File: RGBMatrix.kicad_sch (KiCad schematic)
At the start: 245 parts, among them Q17 PNP, Q18 PNP, Q19 PNP, Q20 PNP, Q21 PNP, Q22 PNP, Q23 PNP, Q24 PNP, Q25 PNP, Q26 PNP, Q27 PNP, Q28 PNP, Q29 PNP, Q30 PNP, Q31 PNP, Q32 PNP, U1 74LS596, U2 74LS596, U3 74LS596, U4 74LS596, U5 74LS596, U6 74LS596, U8 74LS596, U9 74LS596

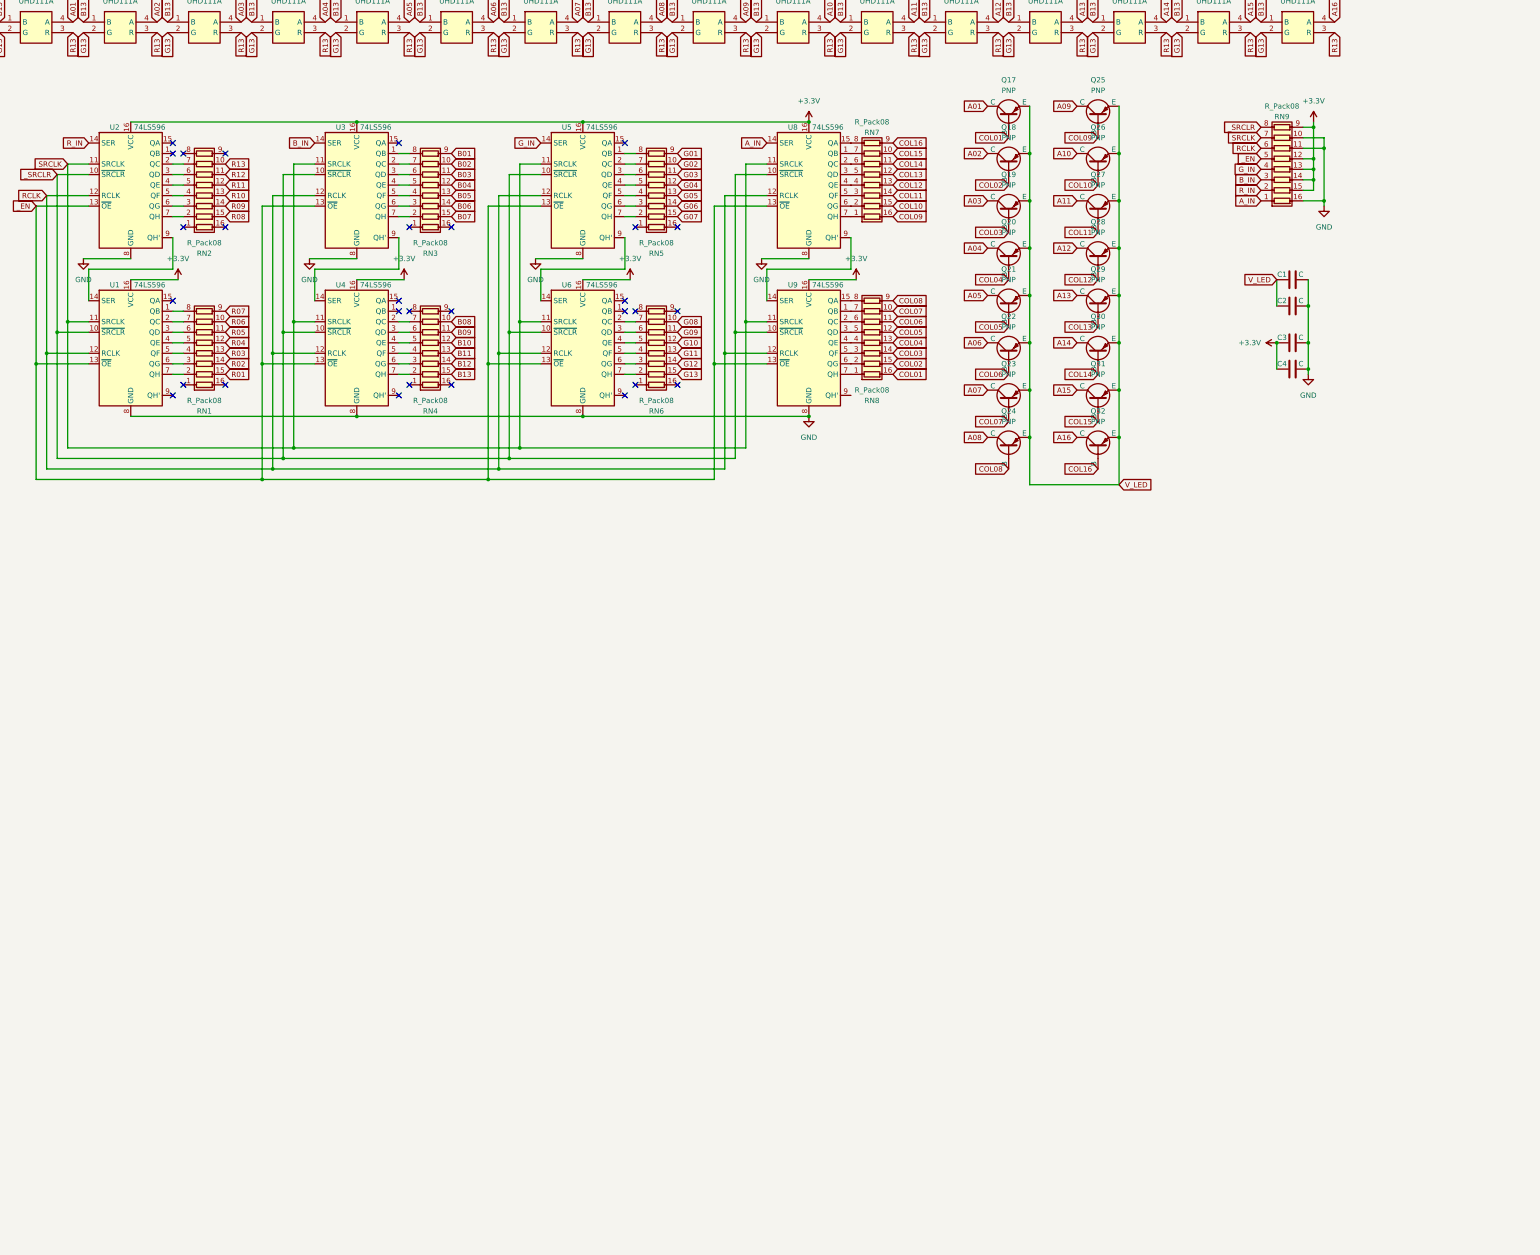
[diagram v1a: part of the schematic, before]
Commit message: High side switch, capacitors
replace fet-s with high side switches
added capacitors for every Shift Register power pin
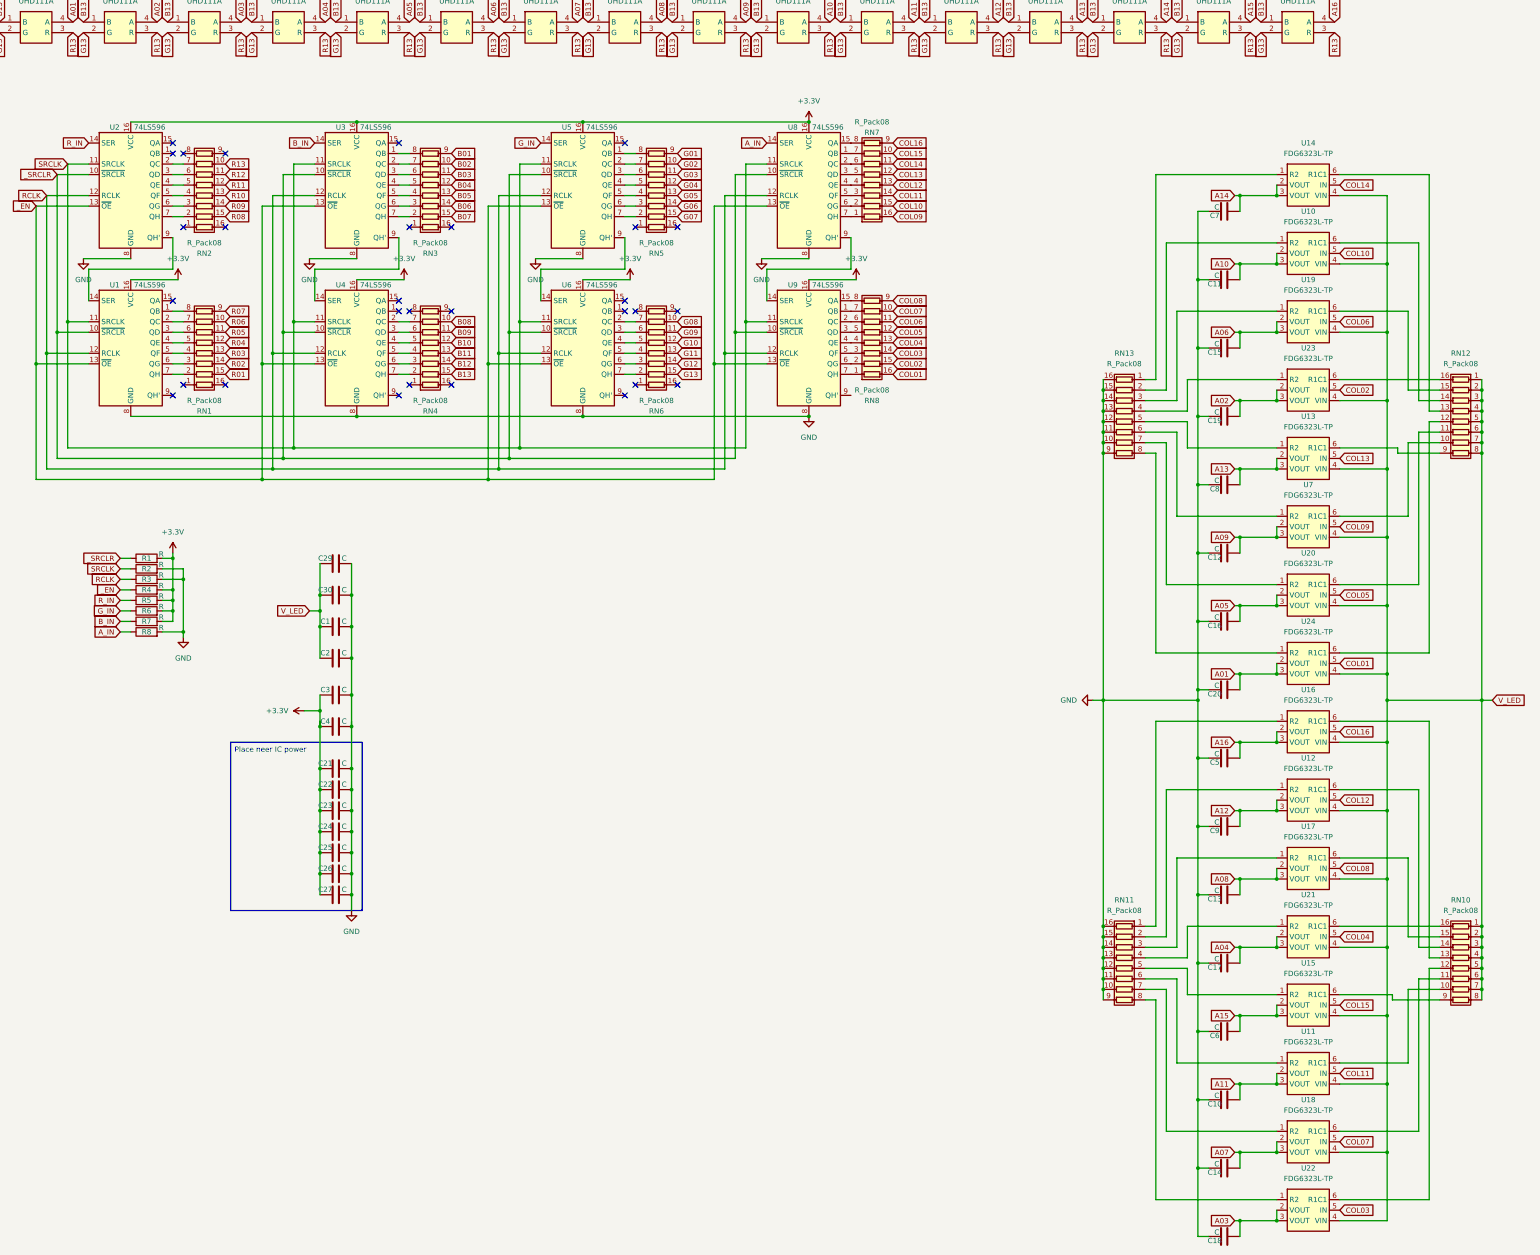
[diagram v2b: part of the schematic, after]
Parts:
- removed Q17, Q18, Q19, Q20, Q21, Q22, Q23, Q24, Q25, Q26, Q27, Q28, Q29, Q30, Q31, Q32: PNP, Package_TO_SOT_SMD:SOT-323_SC-70, symbol Simulation_SPICE:PNP
- removed RN9: R_Pack08, Resistor_SMD:R_Array_Convex_8x0602, symbol Device:R_Pack08
- added C10, C11, C12, C13, C14, C15, C16, C17, C18, C19, C20, C21, C22, C23, C24, C25, C26, C27, C5, C6, C7, C8, C9: C, Capacitor_SMD:C_0402_1005Metric, symbol Device:C
- added C29, C30: C, Capacitor_SMD:C_0805_2012Metric, symbol Device:C
- added R1, R2, R3, R4, R5, R6, R7, R8: R, Resistor_SMD:R_0603_1608Metric, symbol Device:R
- added RN10, RN11, RN12, RN13: R_Pack08, Resistor_SMD:R_Array_Convex_8x0602, symbol Device:R_Pack08
- added U10, U11, U12, U13, U14, U15, U16, U17, U18, U19, U20, U21, U22, U23, U24, U7: FDG6323L-TP, FDG6323L:FDG6323L, symbol FDG6323L:FDG6323L-TP
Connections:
- net +3.3V: now also C21.1, C22.1, C23.1, C24.1, C25.1, C26.1, C27.1, R1.2, R4.2, R5.2, R6.2, R7.2
- net A01: now also C20.1, U24.2 (VOUT), U24.3 (VOUT)
- net A02: now also C19.1, U23.2 (VOUT), U23.3 (VOUT)
- net A03: now also C18.1, U22.2 (VOUT), U22.3 (VOUT)
- net A04: now also C17.1, U21.2 (VOUT), U21.3 (VOUT)
- net A05: now also C16.1, U20.2 (VOUT), U20.3 (VOUT)
- net A06: now also C15.1, U19.2 (VOUT), U19.3 (VOUT)
- net A07: now also C14.1, U18.2 (VOUT), U18.3 (VOUT)
- net A08: now also C13.1, U17.2 (VOUT), U17.3 (VOUT)
- net A09: now also C12.1, U7.2 (VOUT), U7.3 (VOUT)
- net A10: now also C11.1, U10.2 (VOUT), U10.3 (VOUT)
- net A11: now also C10.1, U11.2 (VOUT), U11.3 (VOUT)
- net A12: now also C9.1, U12.2 (VOUT), U12.3 (VOUT)
- net A13: now also C8.1, U13.2 (VOUT), U13.3 (VOUT)
- net A14: now also C7.1, U14.2 (VOUT), U14.3 (VOUT)
- net A15: now also C6.1, U15.2 (VOUT), U15.3 (VOUT)
- net A16: now also C5.1, U16.2 (VOUT), U16.3 (VOUT)
- net A_IN: now also R8.1
- net B_IN: now also R7.1
- net COL01: now also U24.5 (IN)
- net COL02: now also U23.5 (IN)
- net COL03: now also U22.5 (IN)
- net COL04: now also U21.5 (IN)
- net COL05: now also U20.5 (IN)
- net COL06: now also U19.5 (IN)
- net COL07: now also U18.5 (IN)
- net COL08: now also U17.5 (IN)
- net COL09: now also U7.5 (IN)
- net COL10: now also U10.5 (IN)
- net COL11: now also U11.5 (IN)
- net COL12: now also U12.5 (IN)
- net COL13: now also U13.5 (IN)
- net COL14: now also U14.5 (IN)
- net COL15: now also U15.5 (IN)
- net COL16: now also U16.5 (IN)
- net GND: now also C10.2, C11.2, C12.2, C13.2, C14.2, C15.2, C16.2, C17.2, C18.2, C19.2, C20.2, C21.2, C22.2, C23.2, C24.2, C25.2, C26.2, C27.2, C29.2, C30.2, C5.2, C6.2, C7.2, C8.2, C9.2, R2.2, R3.2, R8.2, RN11.10 (R7.2), RN11.11 (R6.2), RN11.12 (R5.2), RN11.13 (R4.2), RN11.14 (R3.2), RN11.15 (R2.2), RN11.16 (R1.2), RN11.9 (R8.2), RN13.10 (R7.2), RN13.11 (R6.2), RN13.12 (R5.2), RN13.13 (R4.2), RN13.14 (R3.2), RN13.15 (R2.2), RN13.16 (R1.2), RN13.9 (R8.2)
- net G_IN: now also R6.1
- net RCLK: now also R3.1
- net R_IN: now also R5.1
- net SRCLK: now also R2.1
- net V_LED: now also C29.1, C30.1, RN10.1 (R1.1), RN10.2 (R2.1), RN10.3 (R3.1), RN10.4 (R4.1), RN10.5 (R5.1), RN10.6 (R6.1), RN10.7 (R7.1), RN10.8 (R8.1), RN12.1 (R1.1), RN12.2 (R2.1), RN12.3 (R3.1), RN12.4 (R4.1), RN12.5 (R5.1), RN12.6 (R6.1), RN12.7 (R7.1), RN12.8 (R8.1), U10.4 (VIN), U11.4 (VIN), U12.4 (VIN), U13.4 (VIN), U14.4 (VIN), U15.4 (VIN), U16.4 (VIN), U17.4 (VIN), U18.4 (VIN), U19.4 (VIN), U20.4 (VIN), U21.4 (VIN), U22.4 (VIN), U23.4 (VIN), U24.4 (VIN), U7.4 (VIN)
- net _EN: now also R4.1
- net _SRCLR: now also R1.1
- new net: RN13.6 (R6.1), U7.1 (R2)
- new net: RN12.10 (R7.2), U7.6 (R1C1)
- new net: RN13.1 (R1.1), U14.1 (R2)
- new net: RN13.2 (R2.1), U10.1 (R2)
- new net: RN13.3 (R3.1), U19.1 (R2)
- new net: RN13.4 (R4.1), U23.1 (R2)
- new net: RN13.5 (R5.1), U13.1 (R2)
- new net: RN13.7 (R7.1), U20.1 (R2)
- new net: RN13.8 (R8.1), U24.1 (R2)
- new net: RN12.12 (R5.2), U24.6 (R1C1)
- new net: RN12.14 (R3.2), U10.6 (R1C1)
- new net: RN10.10 (R7.2), U11.6 (R1C1)
- new net: RN10.11 (R6.2), U18.6 (R1C1)
- new net: RN10.12 (R5.2), U22.6 (R1C1)
- new net: RN10.13 (R4.2), U16.6 (R1C1)
- new net: RN10.14 (R3.2), U12.6 (R1C1)
- new net: RN10.15 (R2.2), U17.6 (R1C1)
- new net: RN10.16 (R1.2), U21.6 (R1C1)
- new net: RN10.9 (R8.2), U15.6 (R1C1)
- new net: RN12.9 (R8.2), U13.6 (R1C1)
- new net: RN11.6 (R6.1), U11.1 (R2)
- new net: RN11.7 (R7.1), U18.1 (R2)
- new net: RN11.1 (R1.1), U16.1 (R2)
- new net: RN11.5 (R5.1), U15.1 (R2)
- new net: RN12.11 (R6.2), U20.6 (R1C1)
- new net: RN12.13 (R4.2), U14.6 (R1C1)
- new net: RN12.15 (R2.2), U19.6 (R1C1)
- new net: RN12.16 (R1.2), U23.6 (R1C1)
- new net: RN11.8 (R8.1), U22.1 (R2)
- new net: RN11.3 (R3.1), U17.1 (R2)
- new net: RN11.2 (R2.1), U12.1 (R2)
- new net: RN11.4 (R4.1), U21.1 (R2)
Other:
- moved on the sheet: C1, C2, C3, C4

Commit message: separate anode control
removed control signals pull resistor, added "art", split control for anodes
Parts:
- removed R1, R2, R3, R4, R5, R6, R7, R8: R, Resistor_SMD:R_0603_1608Metric, symbol Device:R
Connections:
- net _EN is gone; now on net GND: U1.13 (~{OE}), U2.13 (~{OE}), U3.13 (~{OE}), U4.13 (~{OE}), U5.13 (~{OE}), U6.13 (~{OE}), U8.13 (~{OE}), U9.13 (~{OE})
- net RCLK renamed RCLK_RGB
- net RCLK_RGB: no longer U8.12 (RCLK), U9.12 (RCLK)
- net SRCLK renamed SRCLK_RGB
- net SRCLK_RGB: no longer U8.11 (SRCLK), U9.11 (SRCLK)
- net _SRCLR renamed _SRCLR_RGB
- net _SRCLR_RGB: no longer U8.10 (~{SRCLR}), U9.10 (~{SRCLR})
- new net RCLK_A: U8.12 (RCLK), U9.12 (RCLK)
- new net SRCLK_A: U8.11 (SRCLK), U9.11 (SRCLK)
- new net _SRCLR_A: U8.10 (~{SRCLR}), U9.10 (~{SRCLR})
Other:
- moved on the sheet: C10, C11, C12, C13, C14, C15, C16, C17, C18, C19, C20, C5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

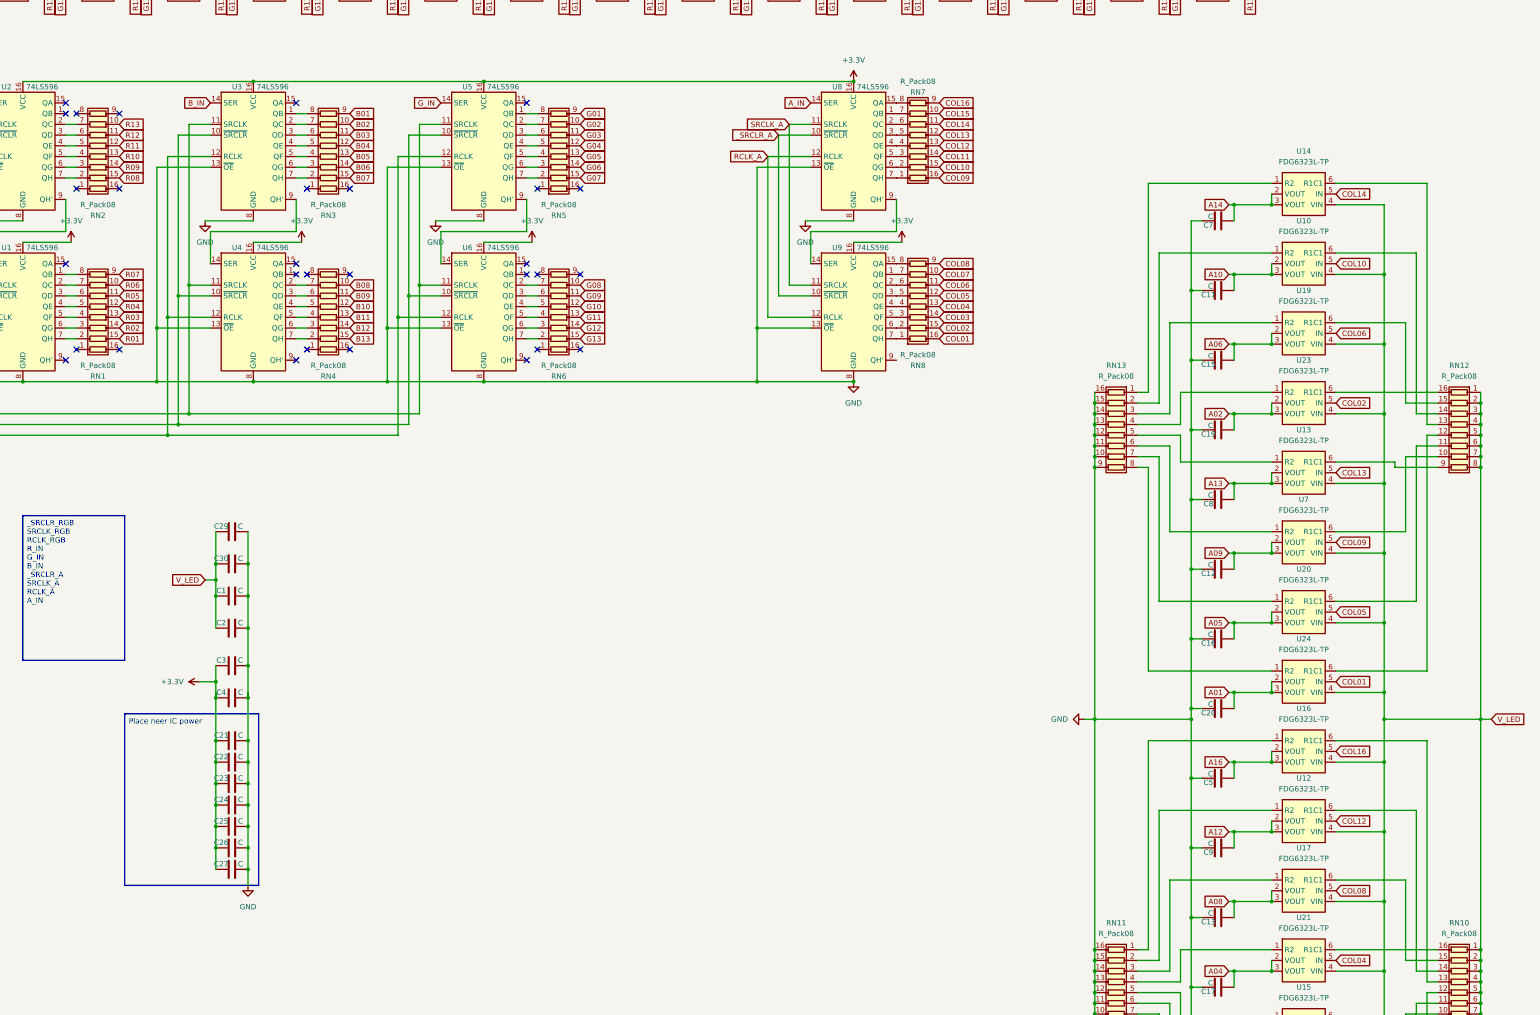
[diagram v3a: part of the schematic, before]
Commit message: update
design, values to resistors
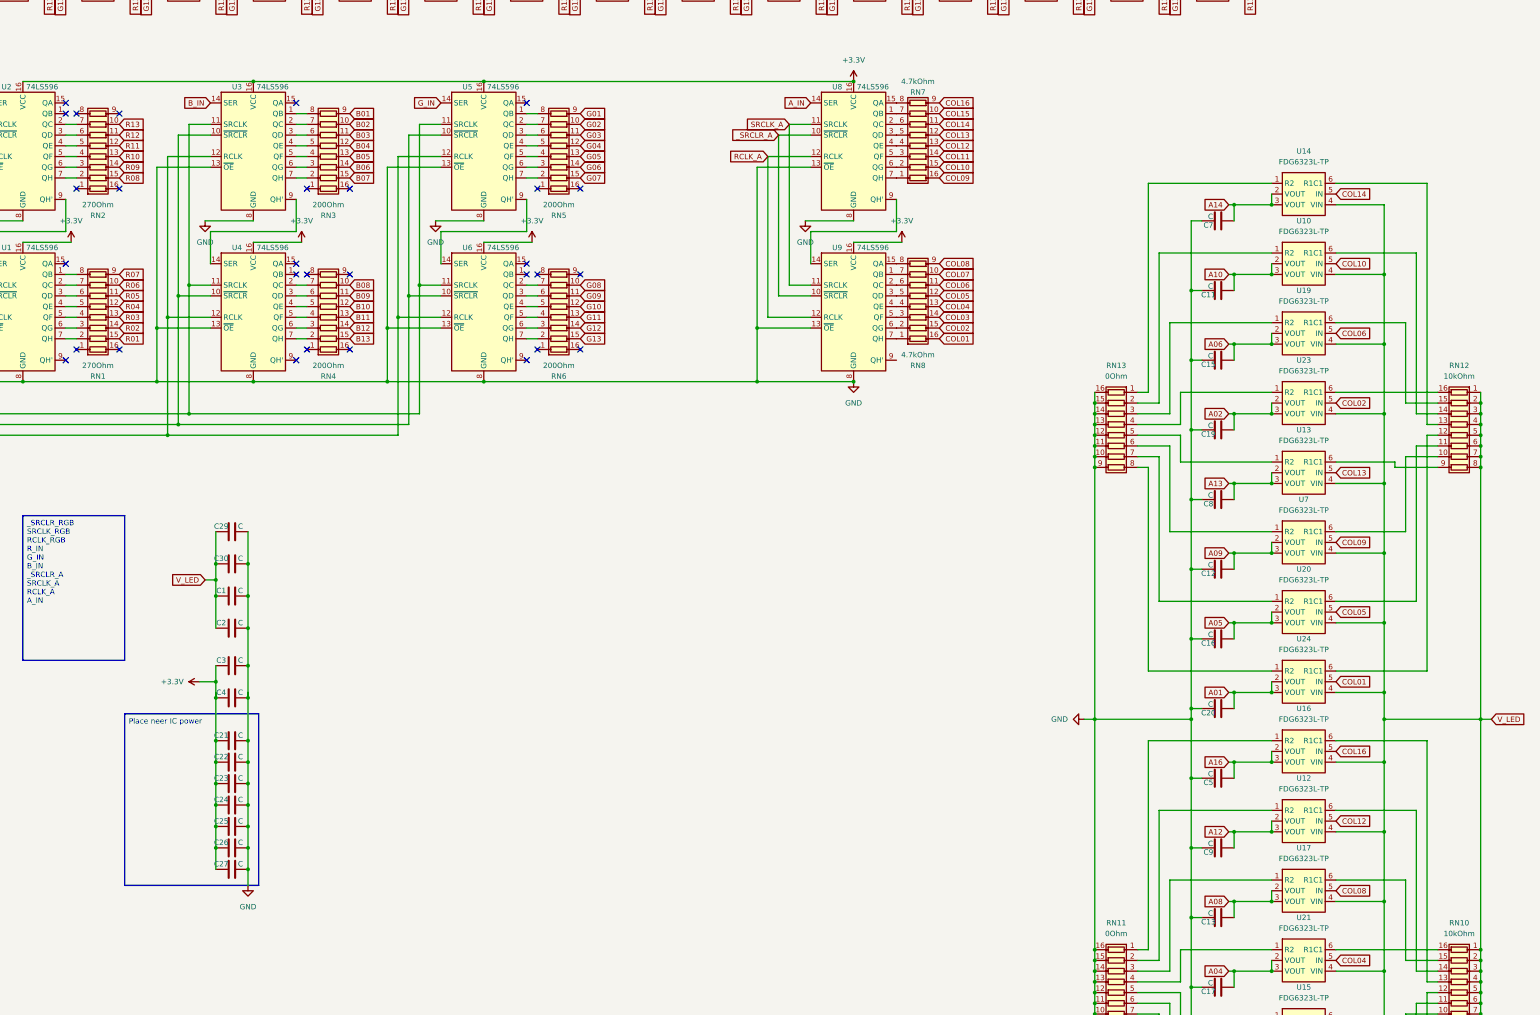
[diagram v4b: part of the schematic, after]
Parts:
- RN1, RN2: value R_Pack08 -> 270Ohm
- RN10, RN12: value R_Pack08 -> 10kOhm
- RN11, RN13: value R_Pack08 -> 0Ohm
- RN3, RN4, RN5, RN6: value R_Pack08 -> 200Ohm
- RN7, RN8: value R_Pack08 -> 4.7kOhm
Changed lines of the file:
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@@
 			)
 		)
-		(property "Value" "R_Pack08"
+		(property "Value" "200Ohm"
 			(at 175.26 271.78 90)
 			(effects
@@
 			)
 		)
-		(property "Value" "R_Pack08"
+		(property "Value" "0Ohm"
 			(at 307.34 312.42 90)
 			(effects
@@
 			)
 		)
-		(property "Value" "R_Pack08"
+		(property "Value" "10kOhm"
 			(at 388.62 444.5 90)
 			(effects
@@
 			)
 		)
-		(property "Value" "R_Pack08"
+		(property "Value" "200Ohm"
 			(at 120.65 271.78 90)
 			(effects
@@
 			)
 		)
-		(property "Value" "R_Pack08"
+		(property "Value" "200Ohm"
 			(at 175.26 309.88 90)
 			(effects
@@
 			)
 		)
-		(property "Value" "R_Pack08"
+		(property "Value" "10kOhm"
 			(at 388.62 312.42 90)
 			(effects
@@
 			)
 		)
-		(property "Value" "R_Pack08"
+		(property "Value" "270Ohm"
 			(at 66.04 309.88 90)
 			(effects
@@
 			)
 		)
-		(property "Value" "R_Pack08"
+		(property "Value" "200Ohm"
 			(at 120.65 309.88 90)
 			(effects
@@
 			)
 		)
-		(property "Value" "R_Pack08"
+		(property "Value" "4.7kOhm"
 			(at 260.35 242.57 90)
 			(effects
@@
 			)
 		)
-		(property "Value" "R_Pack08"
+		(property "Value" "4.7kOhm"
 			(at 260.35 307.34 90)
 			(effects
@@
 			)
 		)
-		(property "Value" "R_Pack08"
+		(property "Value" "270Ohm"
 			(at 66.04 271.78 90)
 			(effects
@@
 			)
 		)
-		(property "Value" "R_Pack08"
+		(property "Value" "0Ohm"
 			(at 307.34 444.5 90)
 			(effects
